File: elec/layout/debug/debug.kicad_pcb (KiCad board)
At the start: 2 copper layers, 225.7 x 100.8 mm, 0 parts

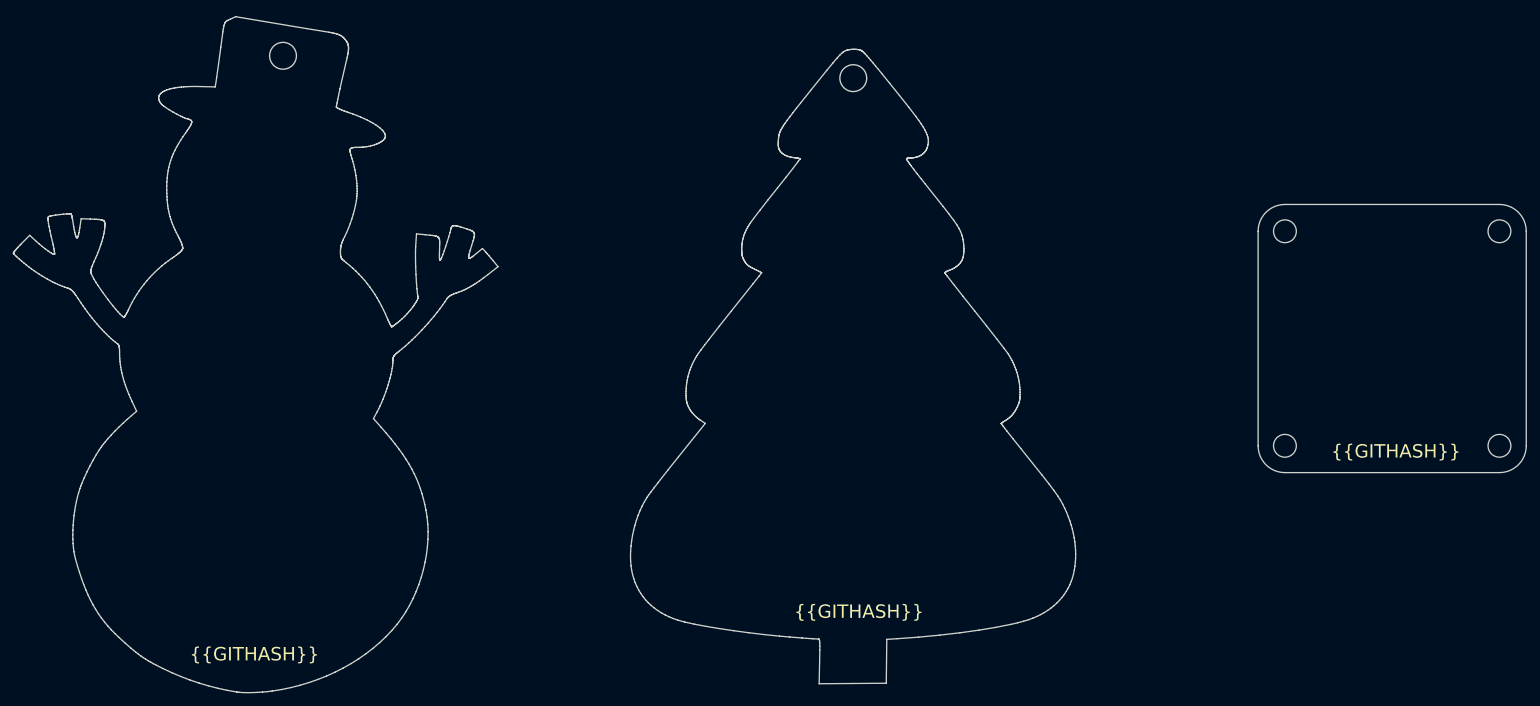
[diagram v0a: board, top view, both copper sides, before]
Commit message: layout 80% complete
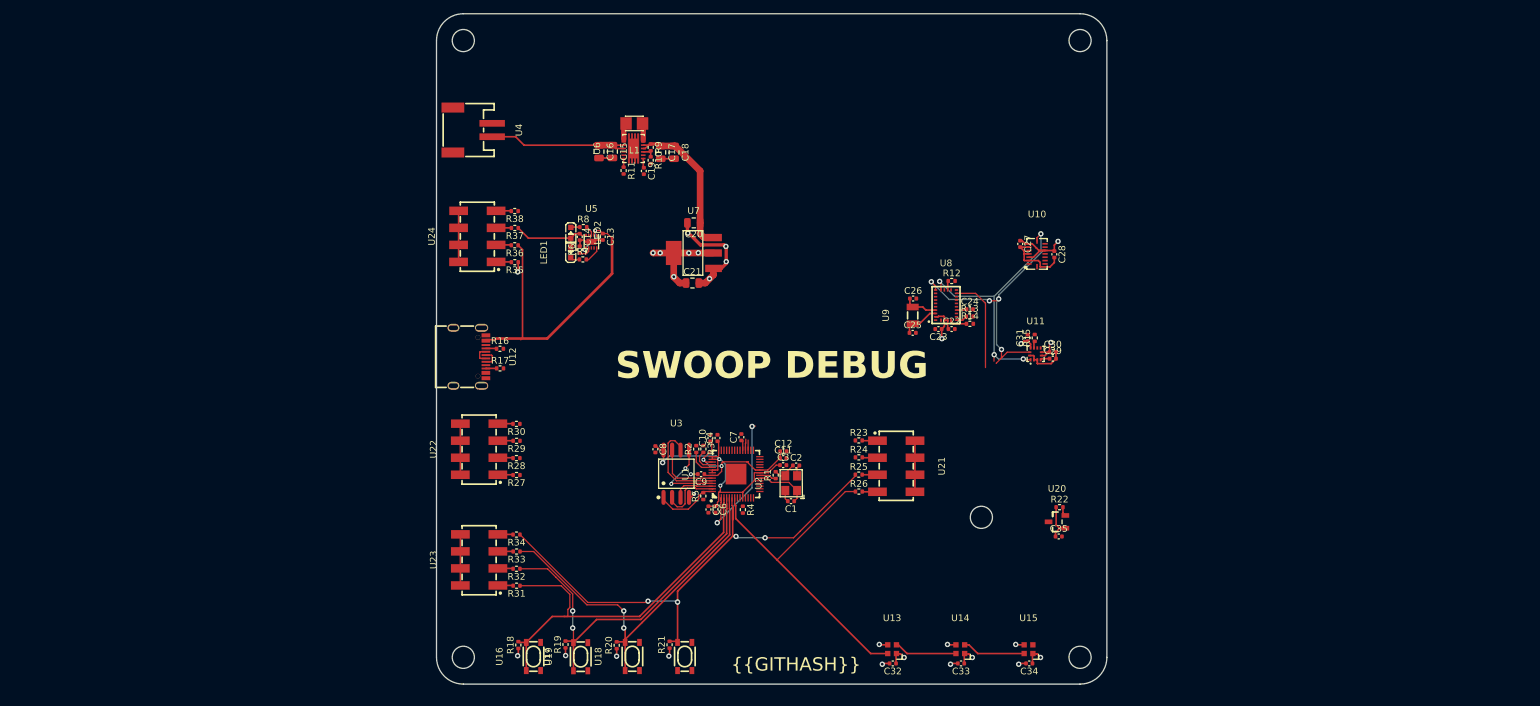
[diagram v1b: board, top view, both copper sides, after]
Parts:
- added C1: 50V 20pF C0G ±5% 0402 Multilayer Ceramic Capacitors MLCC - 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, lib:C0402, F.Cu at (151.9, 122.1)
- added C10: 16V 100nF X7R ±10% 0402 Multilayer Ceramic Capacitors MLCC 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, lib:C0402, F.Cu at (139.9, 112.6)
- added C11: 16V 100nF X7R ±10% 0402 Multilayer Ceramic Capacitors MLCC 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, lib:C0402, F.Cu at (150.8, 115.6)
- added C12: 25V 1uF X5R ±10% 0402 Multilayer Ceramic Capacitors MLCC - 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, lib:C0402, F.Cu at (150.8, 114.6)
- added C13: 25V 1uF X5R ±10% 0402 Multilayer Ceramic Capacitors MLCC - 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, lib:C0402, F.Cu at (123.9, 82.6)
- added C14: 25V 1uF X5R ±10% 0402 Multilayer Ceramic Capacitors MLCC - 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, lib:C0402, F.Cu at (120.4, 82.6)
- added C15: 25V 10uF X5R ±10% 0805 Multilayer Ceramic Capacitors MLCC -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, lib:C0805, F.Cu at (125.3, 69.9)
- added C16: 25V 10uF X5R ±10% 0805 Multilayer Ceramic Capacitors MLCC -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, lib:C0805, F.Cu at (123.3, 69.9)
- added C17: 25V 10uF X5R ±10% 0805 Multilayer Ceramic Capacitors MLCC -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, lib:C0805, F.Cu at (132.5, 70.0)
- added C18: 25V 10uF X5R ±10% 0805 Multilayer Ceramic Capacitors MLCC -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, lib:C0805, F.Cu at (134.5, 70.0)
- added C19: 16V 100nF X7R ±10% 0402 Multilayer Ceramic Capacitors MLCC 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, lib:C0402, F.Cu at (130.0, 72.8)
- added C2: 50V 20pF C0G ±5% 0402 Multilayer Ceramic Capacitors MLCC - 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, lib:C0402, F.Cu at (152.7, 116.7)
- added C20: 25V 10uF X5R ±10% 0805 Multilayer Ceramic Capacitors MLCC -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, lib:C0805, F.Cu at (137.4, 80.5)
- added C21: 25V 10uF X5R ±10% 0805 Multilayer Ceramic Capacitors MLCC -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, lib:C0805, F.Cu at (137.2, 89.5)
- added C22: 16V 100nF X7R ±10% 0402 Multilayer Ceramic Capacitors MLCC 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, lib:C0402, F.Cu at (175.9, 96.4)
- added C23: 25V 1uF X5R ±10% 0402 Multilayer Ceramic Capacitors MLCC - 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, lib:C0402, F.Cu at (173.9, 96.4)
- added C24: 16V 100nF X7R ±10% 0402 Multilayer Ceramic Capacitors MLCC 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, lib:C0402, F.Cu at (178.6, 93.4)
- added C25: 50V 22pF C0G ±5% 0402 Multilayer Ceramic Capacitors MLCC - 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, lib:C0402, F.Cu at (170.1, 96.9)
- added C26: 50V 22pF C0G ±5% 0402 Multilayer Ceramic Capacitors MLCC - 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, lib:C0402, F.Cu at (170.2, 91.8)
- added C27: 16V 100nF X7R ±10% 0402 Multilayer Ceramic Capacitors MLCC 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, lib:C0402, F.Cu at (186.1, 83.7)
- added C28: 16V 100nF X7R ±10% 0402 Multilayer Ceramic Capacitors MLCC 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, lib:C0402, F.Cu at (191.2, 85.2)
- added C29: 16V 100nF X7R ±10% 0402 Multilayer Ceramic Capacitors MLCC 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, lib:C0402, F.Cu at (191.0, 100.8)
- added C3: 16V 100nF X7R ±10% 0402 Multilayer Ceramic Capacitors MLCC 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, lib:C0402, F.Cu at (150.8, 116.7)
- added C30: 25V 1uF X5R ±10% 0402 Multilayer Ceramic Capacitors MLCC - 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, lib:C0402, F.Cu at (191.0, 99.8)
- added C31: 16V 100nF X7R ±10% 0402 Multilayer Ceramic Capacitors MLCC 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, lib:C0402, F.Cu at (187.3, 97.7)
- added C32: 16V 100nF X7R ±10% 0402 Multilayer Ceramic Capacitors MLCC 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, lib:C0402, F.Cu at (167.1, 146.3)
- added C33: 16V 100nF X7R ±10% 0402 Multilayer Ceramic Capacitors MLCC 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, lib:C0402, F.Cu at (177.3, 146.3)
- added C34: 16V 100nF X7R ±10% 0402 Multilayer Ceramic Capacitors MLCC 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, lib:C0402, F.Cu at (187.5, 146.3)
- added C35: 16V 100nF X7R ±10% 0402 Multilayer Ceramic Capacitors MLCC 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, lib:C0402, F.Cu at (191.9, 127.3)
- added C4: 16V 100nF X7R ±10% 0402 Multilayer Ceramic Capacitors MLCC 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, lib:C0402, F.Cu at (141.0, 112.6)
- added C5: 16V 100nF X7R ±10% 0402 Multilayer Ceramic Capacitors MLCC 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, lib:C0402, F.Cu at (139.6, 123.3)
- added C6: 16V 100nF X7R ±10% 0402 Multilayer Ceramic Capacitors MLCC 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, lib:C0402, F.Cu at (140.7, 123.3)
- added C7: 16V 100nF X7R ±10% 0402 Multilayer Ceramic Capacitors MLCC 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, lib:C0402, F.Cu at (144.5, 112.5)
- added C8: 25V 1uF X5R ±10% 0402 Multilayer Ceramic Capacitors MLCC - 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, lib:C0402, F.Cu at (131.7, 114.3)
- added C9: 16V 100nF X7R ±10% 0402 Multilayer Ceramic Capacitors MLCC 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, lib:C0402, F.Cu at (138.5, 118.0)
- added L1: , lib:IND-SMD_L2.5-W2.0_WPN252012H, F.Cu at (128.6, 65.7)
- added LED1: , lib:LED0603-RD, F.Cu at (119.1, 84.9)
- added LED2: , lib:LED0603-RD, F.Cu at (119.1, 82.0)
- added R1: 62.5mW Thick Film Resistors ±100ppm/℃ ±1% 1kΩ 0402 Chip Res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, lib:R0402, F.Cu at (149.7, 118.2)
- added R10: 62.5mW Thick Film Resistors ±100ppm/℃ ±1% 180kΩ 0402 Chip R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, lib:R0402, F.Cu at (131.0, 71.2)
- added R11: 62.5mW Thick Film Resistors ±100ppm/℃ ±1% 1MΩ 0402 Chip Res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, lib:R0402, F.Cu at (127.0, 72.7)
- added R12: 62.5mW Thick Film Resistors ±100ppm/℃ ±1% 10kΩ 0402 Chip Re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, lib:R0402, F.Cu at (175.9, 89.2)
- added R13: 62.5mW Thick Film Resistors ±100ppm/℃ ±1% 10kΩ 0402 Chip Re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, lib:R0402, F.Cu at (178.6, 94.5)
- added R14: 62.5mW Thick Film Resistors ±100ppm/℃ ±1% 10kΩ 0402 Chip Re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, lib:R0402, F.Cu at (178.6, 95.6)
- added R15: 62.5mW Thick Film Resistors ±100ppm/℃ ±1% 1kΩ 0402 Chip Res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, lib:R0402, F.Cu at (188.3, 97.7)
- added R16: 62.5mW Thick Film Resistors ±100ppm/℃ ±1% 5.1kΩ 0402 Chip R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, lib:R0402, F.Cu at (108.5, 99.3)
- added R17: 62.5mW Thick Film Resistors ±100ppm/℃ ±1% 5.1kΩ 0402 Chip R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, lib:R0402, F.Cu at (108.5, 102.2)
- added R18: 62.5mW Thick Film Resistors ±100ppm/℃ ±1% 10kΩ 0402 Chip Re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, lib:R0402, F.Cu at (111.3, 143.5)
- added R19: 62.5mW Thick Film Resistors ±100ppm/℃ ±1% 10kΩ 0402 Chip Re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, lib:R0402, F.Cu at (118.3, 143.4)
- added R2: 62.5mW Thick Film Resistors ±100ppm/℃ ±1% 27kΩ 0402 Chip Re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, lib:R0402, F.Cu at (137.8, 114.3)
- added R20: 62.5mW Thick Film Resistors ±100ppm/℃ ±1% 10kΩ 0402 Chip Re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, lib:R0402, F.Cu at (125.9, 143.5)
- added R21: 62.5mW Thick Film Resistors ±100ppm/℃ ±1% 10kΩ 0402 Chip Re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, lib:R0402, F.Cu at (133.8, 143.5)
- added R22: 62.5mW Thick Film Resistors ±100ppm/℃ ±1% 1kΩ 0402 Chip Res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, lib:R0402, F.Cu at (192.0, 122.9)
- added R23: 62.5mW Thick Film Resistors ±100ppm/℃ ±1% 1kΩ 0402 Chip Res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, lib:R0402, F.Cu at (162.1, 113.0)
- added R24: 62.5mW Thick Film Resistors ±100ppm/℃ ±1% 1kΩ 0402 Chip Res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, lib:R0402, F.Cu at (162.1, 115.5)
- added R25: 62.5mW Thick Film Resistors ±100ppm/℃ ±1% 1kΩ 0402 Chip Res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, lib:R0402, F.Cu at (162.0, 118.1)
- added R26: 62.5mW Thick Film Resistors ±100ppm/℃ ±1% 1kΩ 0402 Chip Res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, lib:R0402, F.Cu at (162.1, 120.6)
- added R27: 62.5mW Thick Film Resistors ±100ppm/℃ ±1% 1kΩ 0402 Chip Res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, lib:R0402, F.Cu at (111.0, 118.2)
- added R28: 62.5mW Thick Film Resistors ±100ppm/℃ ±1% 1kΩ 0402 Chip Res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, lib:R0402, F.Cu at (111.0, 115.6)
- added R29: 62.5mW Thick Film Resistors ±100ppm/℃ ±1% 1kΩ 0402 Chip Res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, lib:R0402, F.Cu at (111.0, 113.0)
- added R3: 62.5mW Thick Film Resistors ±100ppm/℃ ±1% 27kΩ 0402 Chip Re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, lib:R0402, F.Cu at (138.9, 114.3)
- added R30: 62.5mW Thick Film Resistors ±100ppm/℃ ±1% 1kΩ 0402 Chip Res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, lib:R0402, F.Cu at (111.0, 110.5)
- added R31: 62.5mW Thick Film Resistors ±100ppm/℃ ±1% 1kΩ 0402 Chip Res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, lib:R0402, F.Cu at (111.0, 134.7)
- added R32: 62.5mW Thick Film Resistors ±100ppm/℃ ±1% 1kΩ 0402 Chip Res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, lib:R0402, F.Cu at (111.0, 132.1)
- added R33: 62.5mW Thick Film Resistors ±100ppm/℃ ±1% 1kΩ 0402 Chip Res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, lib:R0402, F.Cu at (111.0, 129.6)
- added R34: 62.5mW Thick Film Resistors ±100ppm/℃ ±1% 1kΩ 0402 Chip Res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, lib:R0402, F.Cu at (111.0, 127.0)
- added R35: 62.5mW Thick Film Resistors ±100ppm/℃ ±1% 1kΩ 0402 Chip Res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, lib:R0402, F.Cu at (110.7, 86.4)
- added R36: 62.5mW Thick Film Resistors ±100ppm/℃ ±1% 1kΩ 0402 Chip Res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, lib:R0402, F.Cu at (110.7, 83.9)
- added R37: 62.5mW Thick Film Resistors ±100ppm/℃ ±1% 1kΩ 0402 Chip Res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, lib:R0402, F.Cu at (110.7, 81.3)
- added R38: 62.5mW Thick Film Resistors ±100ppm/℃ ±1% 1kΩ 0402 Chip Res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, lib:R0402, F.Cu at (110.7, 78.8)
- added R4: 62.5mW Thick Film Resistors ±100ppm/℃ ±1% 10kΩ 0402 Chip Re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, lib:R0402, F.Cu at (144.8, 123.3)
- added R5: 62.5mW Thick Film Resistors ±100ppm/℃ ±1% 10kΩ 0402 Chip Re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, lib:R0402, F.Cu at (138.9, 121.3)
- added R6: 62.5mW Thick Film Resistors ±100ppm/℃ ±1% 510Ω 0402 Chip Re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, lib:R0402, F.Cu at (120.4, 84.5)
- added R7: 62.5mW Thin Film Resistor ±0.5% ±25ppm/℃ 110Ω 0402 Chip Res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, lib:R0402, F.Cu at (120.9, 86.0)
- added R8: 62.5mW Thick Film Resistors ±100ppm/℃ ±1% 82Ω 0402 Chip Res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, lib:R0402, F.Cu at (121.0, 81.2)
- added R9: 62.5mW Thick Film Resistors ±100ppm/℃ ±1% 1MΩ 0402 Chip Res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, lib:R0402, F.Cu at (131.0, 69.3)
- added U1: , lib:LQFN-56_L7.0-W7.0-P0.4-EP, F.Cu at (143.7, 118.0)
- added U10: , lib:LGA-16_L4.5-W3.0-P0.50-BL, F.Cu at (188.6, 85.2)
- added U11: , lib:LGA-12_L2.0-W2.0-P0.50-BL, F.Cu at (188.4, 100.1)
- added U12: , lib:USB-C-SMD_KH-TYPE-C-16P, F.Cu at (104.0, 100.5)
- added U13: , lib:LED-SMD_4P-L2.0-W2.0-BR, F.Cu at (167.0, 144.1)
- added U14: , lib:LED-SMD_4P-L2.0-W2.0-BR, F.Cu at (177.2, 144.1)
- added U15: , lib:LED-SMD_4P-L2.0-W2.0-BR, F.Cu at (187.4, 144.1)
- added U16: , lib:KEY-SMD_4P-L4.2-W3.2-P2.20-LS4.6, F.Cu at (113.5, 145.2)
- added U17: , lib:KEY-SMD_4P-L4.2-W3.2-P2.20-LS4.6, F.Cu at (120.6, 145.3)
- added U18: , lib:KEY-SMD_4P-L4.2-W3.2-P2.20-LS4.6, F.Cu at (128.3, 145.2)
- added U19: , lib:KEY-SMD_4P-L4.2-W3.2-P2.20-LS4.6, F.Cu at (136.1, 145.2)
- added U2: , lib:OSC-SMD_4P-L3.2-W2.5-BL, F.Cu at (152.0, 119.4)
- added U20: , lib:SOT-23-3_L2.9-W1.3-P1.90-LS2.4-BR-CW, F.Cu at (191.6, 125.1)
- added U21: , lib:HDR-SMD_8P-P2.54-V-M-R2-C4-LS7.4, F.Cu at (167.6, 116.8)
- added U22: , lib:HDR-SMD_8P-P2.54-V-M-R2-C4-LS7.4, F.Cu at (105.4, 114.3)
- added U23: , lib:HDR-SMD_8P-P2.54-V-M-R2-C4-LS7.4, F.Cu at (105.4, 130.8)
- added U24: , lib:HDR-SMD_8P-P2.54-V-M-R2-C4-LS7.4, F.Cu at (105.2, 82.5)
- added U3: , lib:SOIC-8_L5.3-W5.3-P1.27-LS8.0-BL, F.Cu at (134.8, 118.0)
- added U4: , lib:CONN-SMD_P2.00_S2B-PH-SM4-TB-LF-SN, F.Cu at (104.4, 66.7)
- added U5: , lib:WSON-10_L2.0-W2.0-P0.40-BL-EP, F.Cu at (122.2, 83.3)
- added U6: , lib:VSON-14_L4.0-W3.0-P0.50-BL-EP_TI_DSJ, F.Cu at (128.4, 69.4)
- added U7: , lib:SOT-223-3_L6.5-W3.4-P2.30-LS7.0-BR, F.Cu at (137.4, 85.0)
- added U8: , lib:LGA-28_L5.2-W3.8-P0.50-BL, F.Cu at (175.1, 92.8)
- added U9: , lib:FC-135R_L3.2-W1.5, F.Cu at (170.1, 94.3)
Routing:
- net vcc: track 0.00 -> 102.0 mm, vias 0 -> 20
- net gnd: track 0.00 -> 85.0 mm, vias 0 -> 12
- net vcc-1: track 0.00 -> 78.4 mm, vias 0 -> 4
- net vcc-4: track 0.00 -> 58.8 mm
- net vcc-5: track 0.00 -> 57.9 mm, vias 0 -> 2
- net vcc-6: track 0.00 -> 57.5 mm, vias 0 -> 2
- net vcc-8: track 0.00 -> 50.3 mm, vias 0 -> 2
- net vcc-2: track 0.00 -> 50.2 mm
- net scl: track 0.00 -> 41.1 mm, vias 0 -> 4
- net sda: track 0.00 -> 39.9 mm, vias 0 -> 4
- net vcc-3: track 0.00 -> 36.0 mm, vias 0 -> 2
- net vcc-9: track 0.00 -> 35.2 mm
- net vcc-7: track 0.00 -> 23.4 mm, vias 0 -> 2
- net vcc-12: track 0.00 -> 23.2 mm
- net sck: track 0.00 -> 14.4 mm
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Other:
- board size 225.7 x 100.8 mm -> 100 x 100 mm
- board text added: "SWOOP DEBUG"
